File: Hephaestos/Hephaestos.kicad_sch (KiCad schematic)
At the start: 55 parts, among them J1 Conn_01x04, J11 Conn_01x02, J4 Conn_02x05_Counter_Clockwise, U10 AP2205K-3.3, U2 MCP2542FDxMF, U3 AP2205K-5.0, U5 MCP2517FD-xSL, U7 STM32F030C8Tx, Y1 40 MHz 9 pF, Y2 16 MHz 9 pF

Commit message: Downgrade CAN controller to 2.0B for driver compatibility
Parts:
- removed C2, C4, C9: 0.1 uF, Capacitor_SMD:C_0402_1005Metric, symbol Device:C
- removed U2: MCP2542FDxMF, Package_DFN_QFN:DFN-8-1EP_3x3mm_P0.65mm_EP1.55x2.4mm, symbol Interface_CAN_LIN:MCP2542FDxMF
- removed U5: MCP2517FD-xSL, Package_SO:SOIC-14_3.9x8.7mm_P1.27mm, symbol Interface_CAN_LIN:MCP2517FD-xSL
- added C13, C14, C23: 0.1 uF, Capacitor_SMD:C_0402_1005Metric, symbol Device:C
- added R35, R42: 1k, Resistor_SMD:R_0402_1005Metric, symbol Device:R
- added U8: MCP25625-x-SS, Package_SO:SSOP-28_5.3x10.2mm_P0.65mm, symbol Interface_CAN_LIN:MCP25625-x-SS
- renumbered C5 to C10, C17 to C11, C27 to C12, C16 to C15, C6 to C16, C13 to C17, C15 to C19, C19 to C20, C14 to C21, C3 to C22, C8 to C5, C23 to C6, C24 to C7, C10 to C8, C21 to C9, D7 to D10, D12 to D6, D1 to D7, D5 to D8, D6 to D9, F7 to F5, J4 to J5, J11 to J6, J1 to J7, R1 to R27, R18 to R28, R20 to R29, R31 to R30, R37 to R31, R19 to R32, R26 to R33, R27 to R34, R14 to R36, R56 to R37, R21 to R38, R28 to R39, R32 to R40, R15 to R41, U10 to U5, U3 to U6, Y2 to Y1, Y1 to Y2
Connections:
- net +3.3V: now also C14.1, C23.1, R35.1, U8.1 (VIO), U8.19 (VDD)
- net +5V: now also C13.1, U8.27 (VDDA)
- net CANH: now also U8.4 (CANH)
- net CANL: now also U8.3 (CANL)
- net CAN_CLK_A: now also U8.8 (OSC2)
- net CAN_CLK_B: now also U8.9 (OSC1)
- net CAN_CS: now also U8.17 (~{CS})
- net CAN_INT: now also U8.13 (~{INT})
- net CAN_PICO: now also U8.15 (SI)
- net CAN_POCI: now also U8.16 (SO)
- net CAN_SCK: now also U8.14 (SCK)
- net GND: now also C13.2, C14.2, C23.2, R42.1, U8.10 (GND), U8.26 (VSS)
- new net: U8.20 (TxCAN), U8.24 (TXD)
- new net: U8.21 (RxCAN), U8.28 (RXD)
- new net CAN_RST: R35.2, U8.18 (~{RESET})
- new net CAN_STBY: R42.2, U8.5 (STBY)
- no-connect marks 17 -> 20
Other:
- note added: "5v Regulator"
- note added: "CAN Controller/Transciever & Connector"
- note removed: "CAN Transciever & Connector"
- moved on the sheet: C10, C16, C22, C5, C7, D6, D7, F5, J6, J7, JP5, R27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

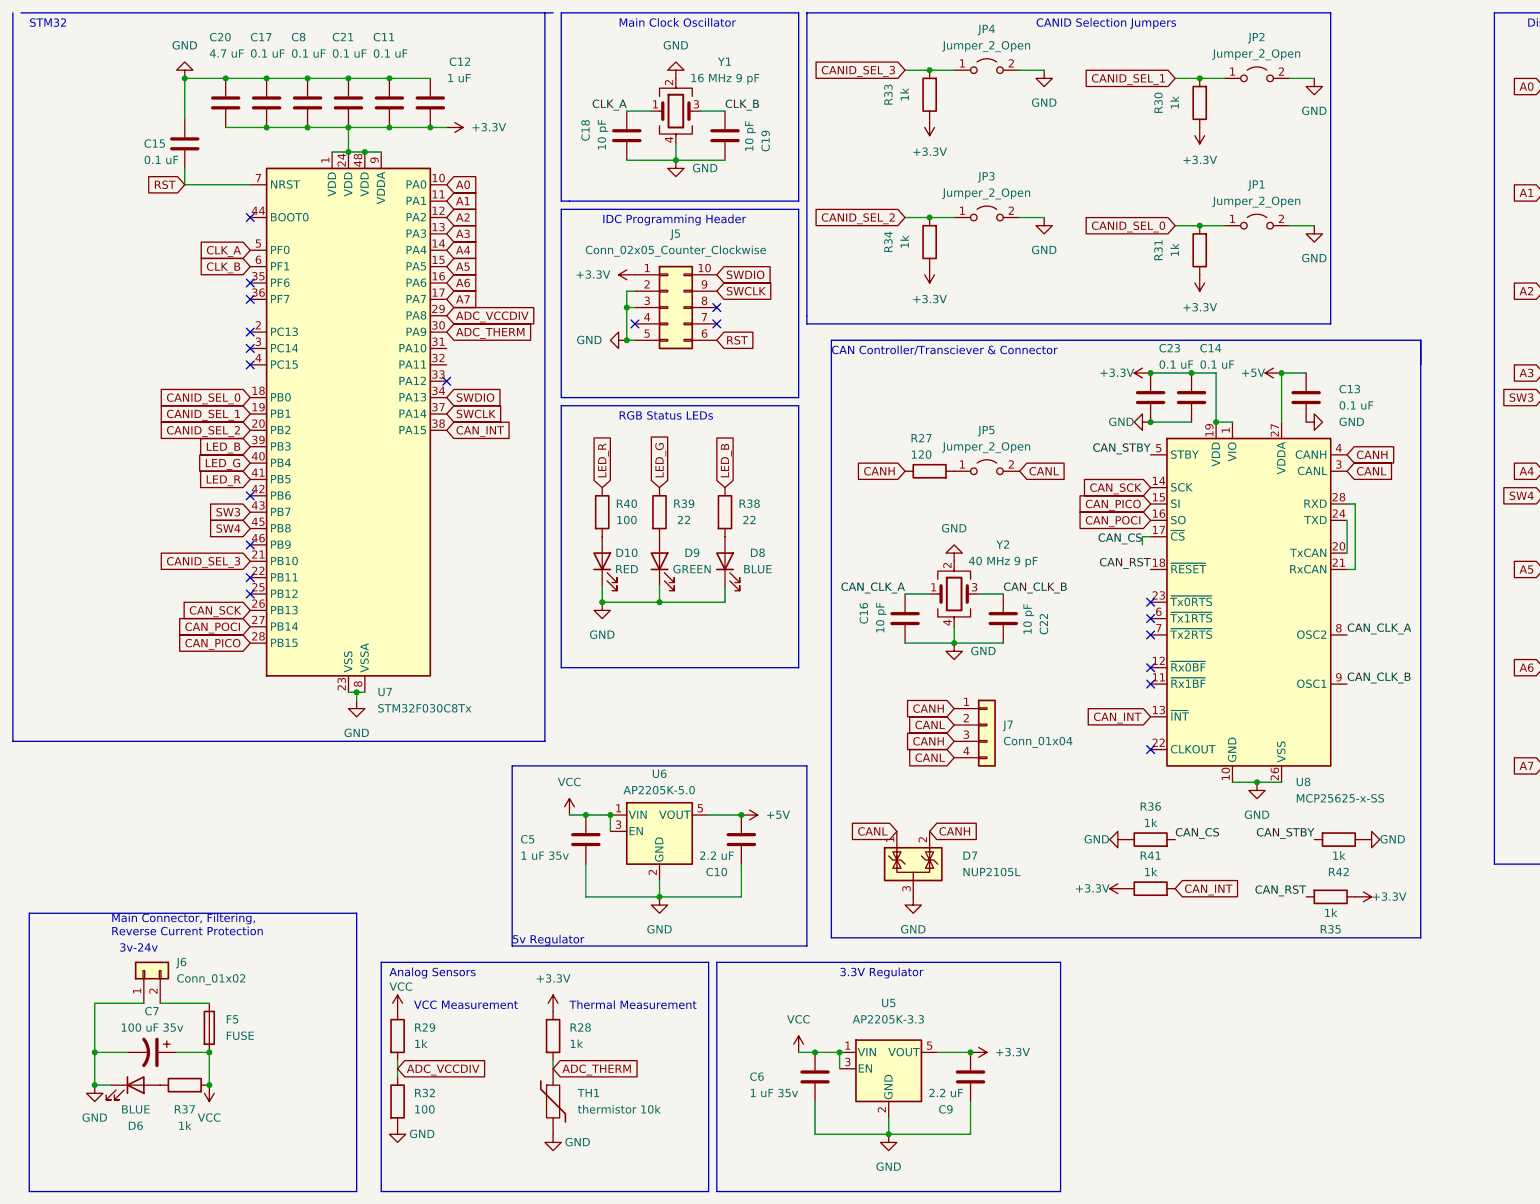
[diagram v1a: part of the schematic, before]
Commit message: Switch to F042 w/ internal CAN controller, change stackup
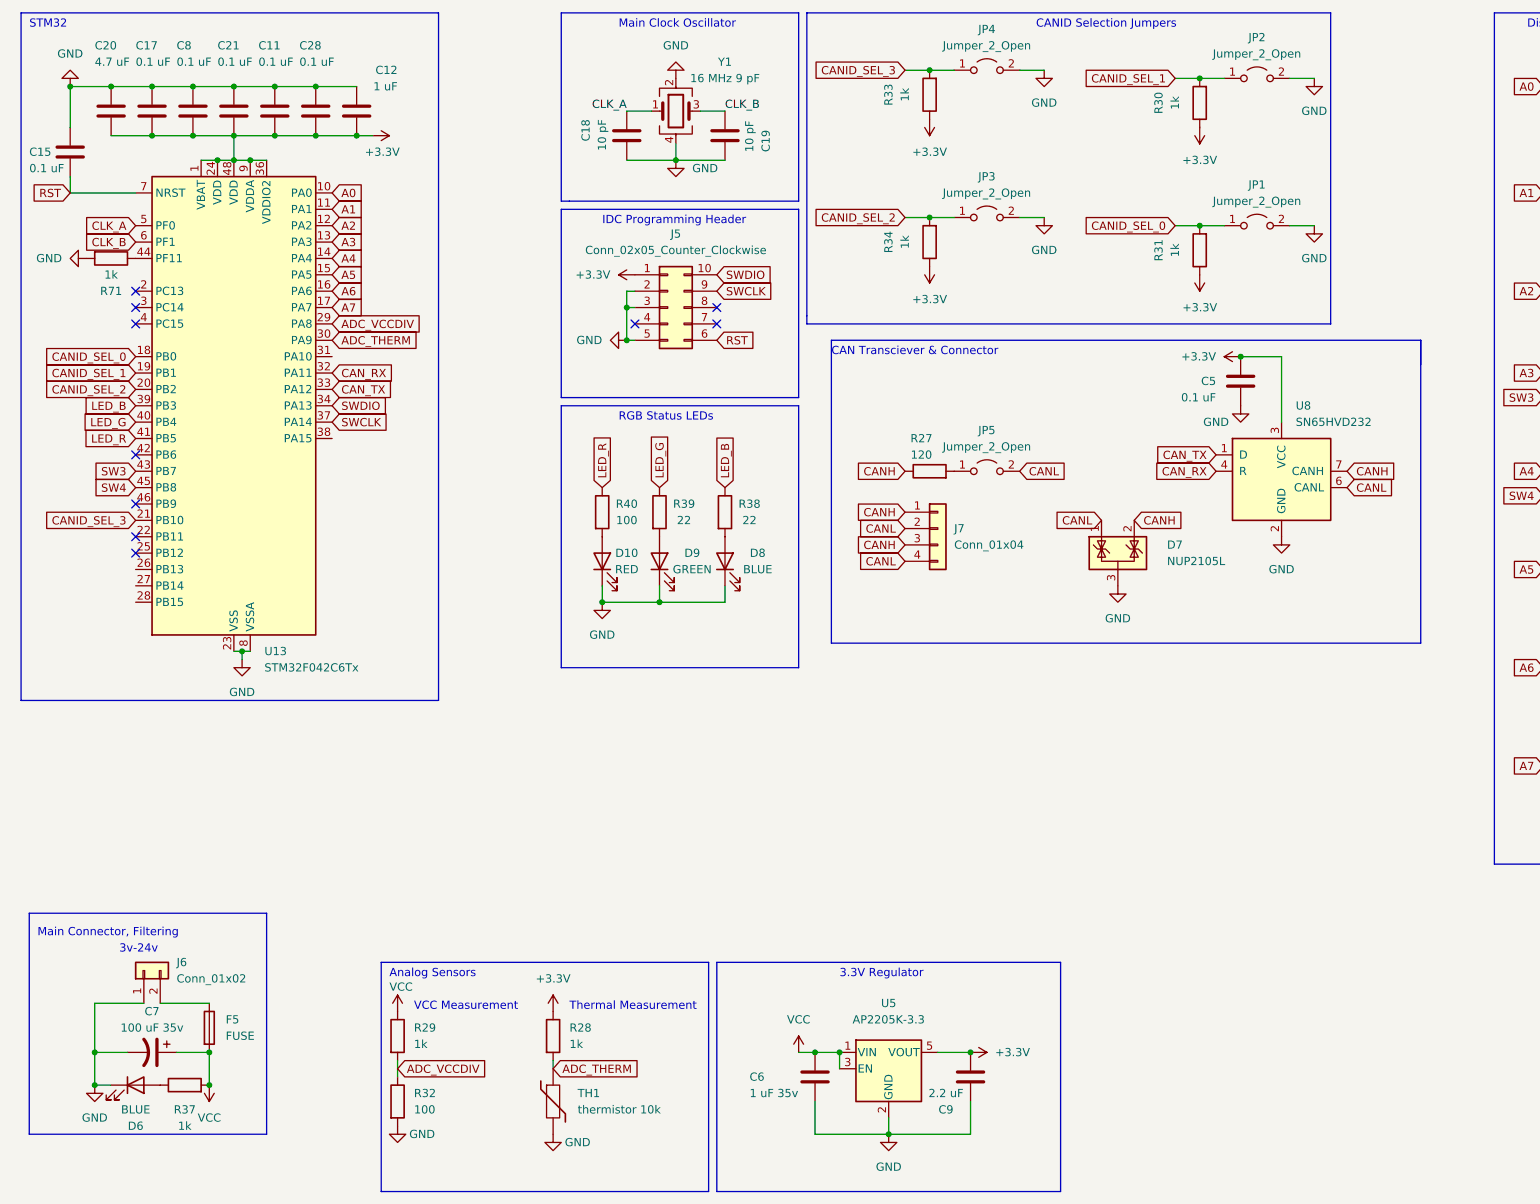
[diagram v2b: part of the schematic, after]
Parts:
- removed C10: 2.2 uF, Capacitor_SMD:C_0603_1608Metric, symbol Device:C
- removed C13, C14, C23: 0.1 uF, Capacitor_SMD:C_0402_1005Metric, symbol Device:C
- removed C16, C22: 10 pF, Capacitor_SMD:C_0402_1005Metric, symbol Device:C
- removed R35, R36, R41, R42: 1k, Resistor_SMD:R_0402_1005Metric, symbol Device:R
- removed U6: AP2205K-5.0, Package_TO_SOT_SMD:SOT-23-5, symbol Regulator_Linear:AP2204K-5.0
- removed U7: STM32F030C8Tx, Package_QFP:LQFP-48_7x7mm_P0.5mm, symbol MCU_ST_STM32F0:STM32F030C8Tx
- removed U8: MCP25625-x-SS, Package_SO:SSOP-28_5.3x10.2mm_P0.65mm, symbol Interface_CAN_LIN:MCP25625-x-SS
- removed Y2: 40 MHz 9 pF, Crystal:Crystal_SMD_3225-4Pin_3.2x2.5mm, symbol Device:Crystal_GND24
- added C28: 0.1 uF, Capacitor_SMD:C_0402_1005Metric, symbol Device:C
- added R71: 1k, Resistor_SMD:R_0402_1005Metric, symbol Device:R
- added U13: STM32F042C6Tx, Package_QFP:LQFP-48_7x7mm_P0.5mm, symbol MCU_ST_STM32F0:STM32F042C6Tx
- added U8: SN65HVD232, Package_SO:SOIC-8_3.9x4.9mm_P1.27mm, symbol Interface_CAN_LIN:SN65HVD232
- C5: value 1 uF 35v -> 0.1 uF; footprint Capacitor_SMD:C_0603_1608Metric -> Capacitor_SMD:C_0402_1005Metric
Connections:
- net +3.3V: now also C5.2, C28.2, U13.1 (VBAT), U13.24 (VDD), U13.36 (VDDIO2), U13.48 (VDD), U13.9 (VDDA), U8.3 (VCC)
- net A0: now also U13.10 (PA0)
- net A1: now also U13.11 (PA1)
- net A2: now also U13.12 (PA2)
- net A3: now also U13.13 (PA3)
- net A4: now also U13.14 (PA4)
- net A5: now also U13.15 (PA5)
- net A6: now also U13.16 (PA6)
- net A7: now also U13.17 (PA7)
- net ADC_THERM: now also U13.30 (PA9)
- net ADC_VCCDIV: now also U13.29 (PA8)
- net CANH: now also U8.7 (CANH)
- net CANID_SEL_0: now also U13.18 (PB0)
- net CANID_SEL_1: now also U13.19 (PB1)
- net CANID_SEL_2: now also U13.20 (PB2)
- net CANID_SEL_3: now also U13.21 (PB10)
- net CANL: now also U8.6 (CANL)
- net CLK_A: now also U13.5 (PF0)
- net CLK_B: now also U13.6 (PF1)
- net GND: now also C5.1, C28.1, R71.2, U13.23 (VSS), U13.35 (VSS), U13.47 (VSS), U13.8 (VSSA), U8.2 (GND); no longer C5.2
- net LED_B: now also U13.39 (PB3)
- net LED_G: now also U13.40 (PB4)
- net LED_R: now also U13.41 (PB5)
- net RST: now also U13.7 (NRST)
- net SW3: now also U13.43 (PB7)
- net SW4: now also U13.45 (PB8)
- net SWCLK: now also U13.37 (PA14)
- net SWDIO: now also U13.34 (PA13)
- net VCC: no longer C5.1
- new net: R71.1, U13.44 (PF11)
- new net CAN_RX: U13.32 (PA11), U8.4 (R)
- new net CAN_TX: U13.33 (PA12), U8.1 (D)
- no-connect marks 20 -> 10
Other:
- note added: "CAN Transciever & Connector"
- note added: "Main Connector, Filtering"
- note removed: "5v Regulator"
- note removed: "CAN Controller/Transciever & Connector"
- note removed: "Main Connector, Filtering, Reverse Current Protection"
- moved on the sheet: C11, C12, C15, C17, C20, C21, C8, D7, J7

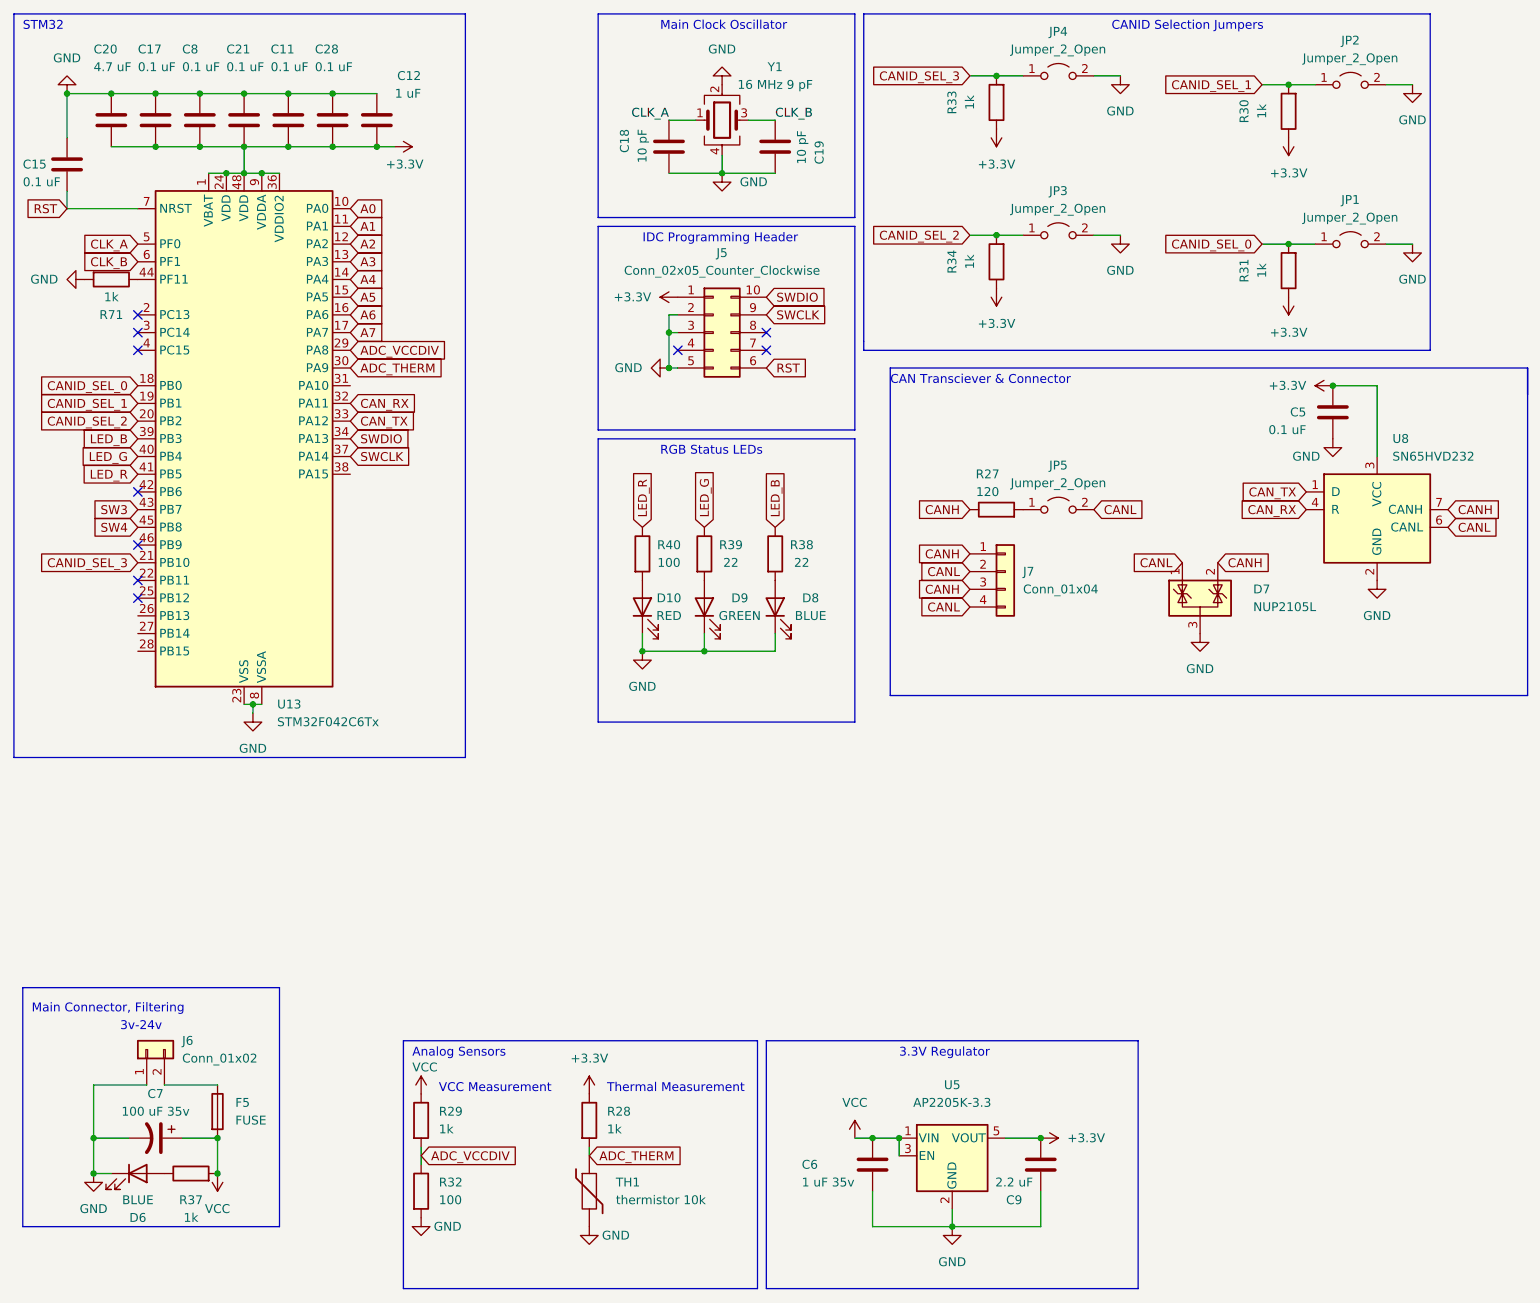
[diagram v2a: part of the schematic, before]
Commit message: Add second bulk cap
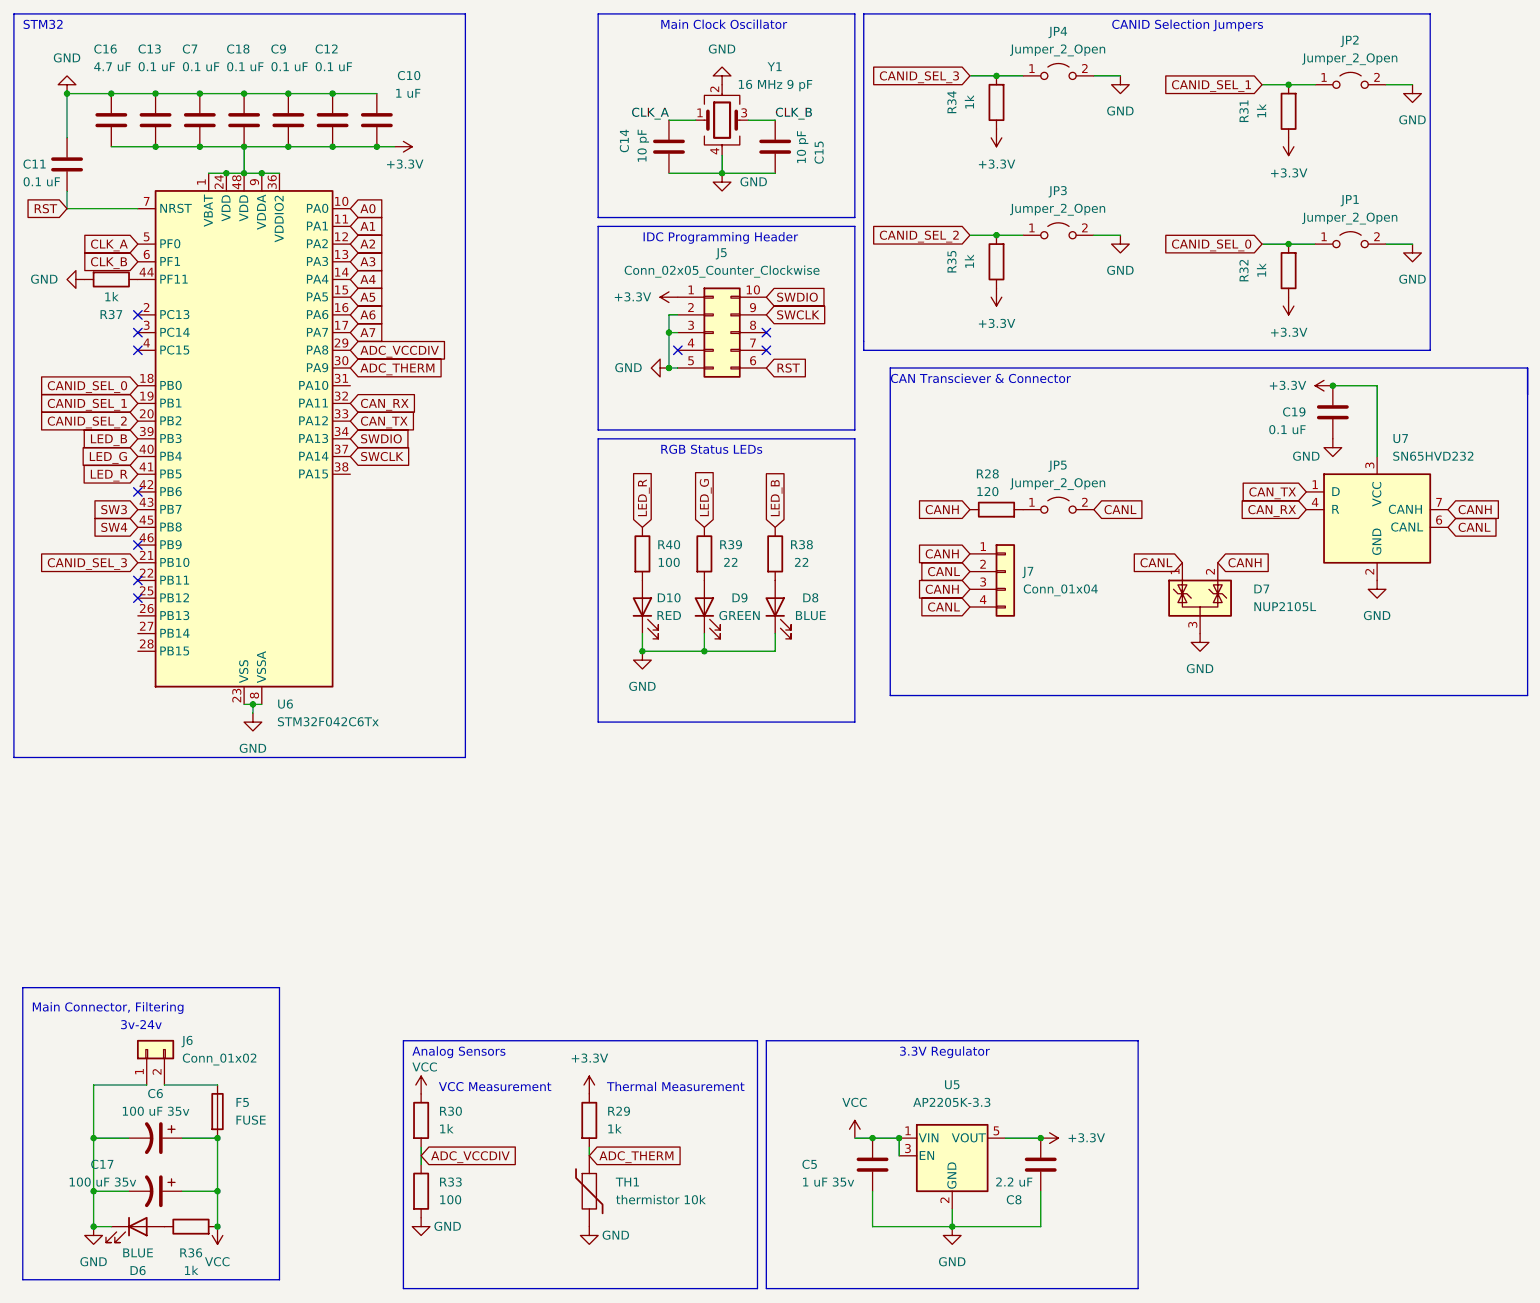
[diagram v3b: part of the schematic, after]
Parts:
- added C17: 100 uF 35v, Capacitor_SMD:CP_Elec_6.3x7.7, symbol Device:C_Polarized_US
- renumbered C12 to C10, C15 to C11, C28 to C12, C17 to C13, C18 to C14, C19 to C15, C20 to C16, C21 to C18, C5 to C19, C6 to C5, C7 to C6, C8 to C7, C9 to C8, C11 to C9, R27 to R28, R28 to R29, R29 to R30, R30 to R31, R31 to R32, R32 to R33, R33 to R34, R34 to R35, R37 to R36, R71 to R37, U13 to U6, U8 to U7
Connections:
- net GND: now also C17.2
- net VCC: now also C17.1
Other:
- moved on the sheet: D6, R36
